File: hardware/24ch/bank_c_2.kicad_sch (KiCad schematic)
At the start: 45 parts, among them U301 AD7124-8BCPZ, U302 ADT7310TRZ, U303 ADT7310TRZ

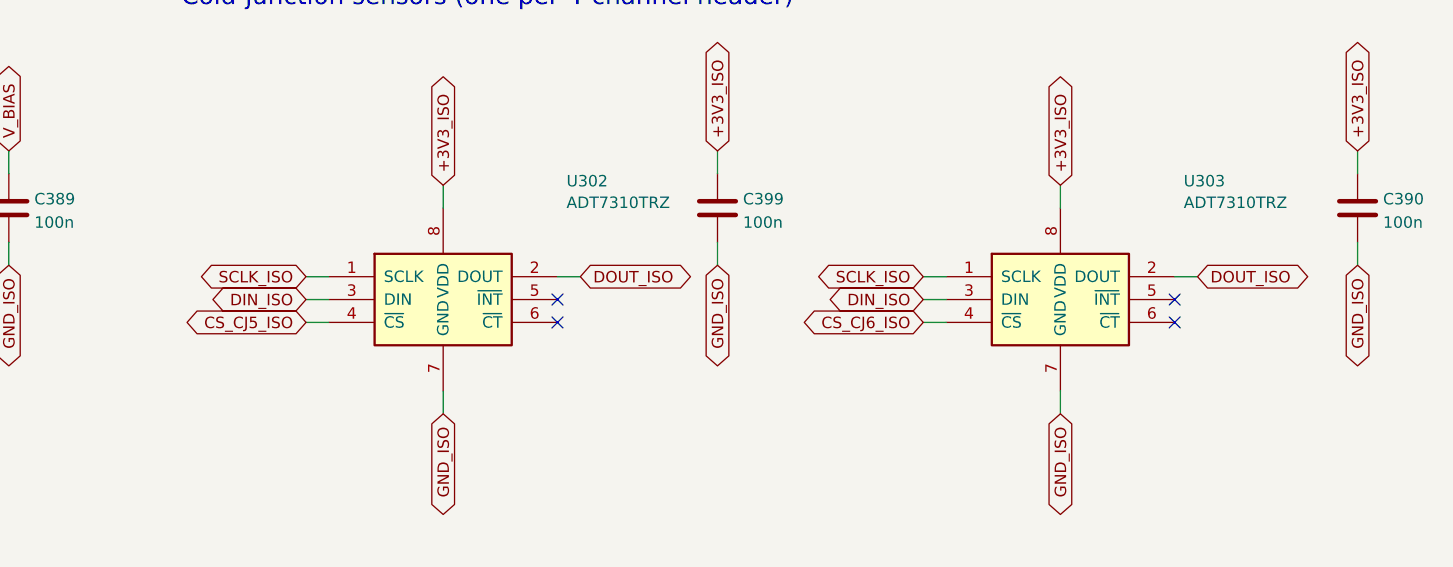
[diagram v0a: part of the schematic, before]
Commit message: 24ch cheaper-parts variant (0036): TMP126, CA-IS3761HW, RS-485 DNP, drop-in swaps
- CJ sensors ADT7310 x6 -> TMP126DCKR (C5219998); R443 22k DIN_ISO-DOUT_ISO for the
  3-wire SIO, R415 removed, ALERT grounded. Sensors moved <= 8 mm to clear spots beside
  their 100 nF (no closer spot to the terminals without touching TC traces, 0035 D2).
- ISO7761 -> CA-IS3761HW (same pinout, 5F/1R, default high); BOCHEN 3296W trimmer;
  SAMWHA 22u 1210.
- RS-485 block DNP: footprints kept; fab.py drops DNP parts from BOM/CPL and writes
  DNP.txt; cost.py skips them. External window watchdog tried and removed (owner).
- gen/delta.py: carry a schematic change onto the routed board (replace/add/remove,
  re-net, DNP, OLD>NEW@DEG reuse); it never deletes another net's track under a pad.
- Board: incremental edits only; analog nets (TC*, V_BIAS, VREF, REF*) identical to
  the pre-0036 board. Gates: ERC 0/0 (471 symbols); fab.py DRC/unconnected/parity
  0/0/0; pincaps 0 over. Parts ~$105 -> ~$72/board (CALCULATIONS 8.1, by hand).
- Docs: decision 0036, CALCULATIONS 8, ISSUES (I-109, I-114, I-119, I-104, I-094,
  new I-123 stock), STATE, 24ch README, superseded.txt.

Co-Authored-By: Claude Opus 5.5 <noreply@anthropic.com>
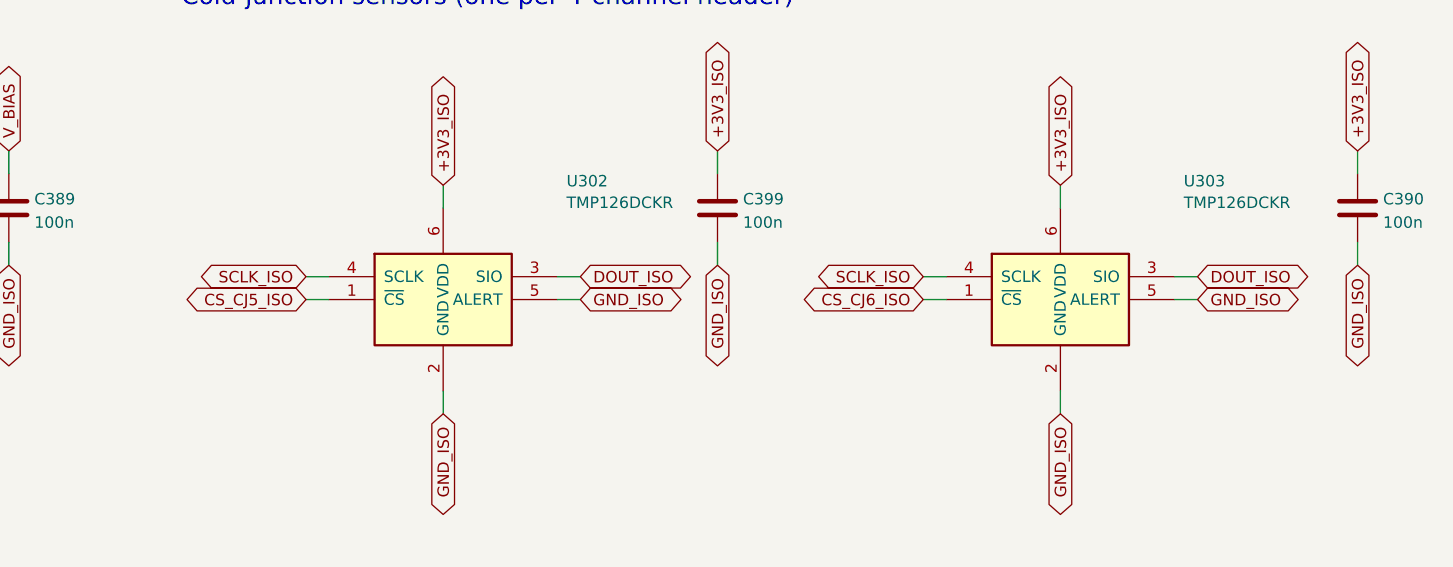
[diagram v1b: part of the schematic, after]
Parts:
- U302, U303: value ADT7310TRZ -> TMP126DCKR; footprint Package_SO:SOIC-8_3.9x4.9mm_P1.27mm -> Package_TO_SOT_SMD:SOT-363_SC-70-6; symbol thermo24:ADT7310 -> thermo24:TMP126; LCSC C578060 -> C5219998; MPN ADT7310TRZ-REEL7 -> TMP126DCKR; Manufacturer ADI -> TI
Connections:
- net +3V3_ISO: now also U302.6 (VDD), U303.6 (VDD); no longer U302.8 (VDD), U303.8 (VDD)
- net CS_CJ5_ISO: now also U302.1 (~{CS}); no longer U302.4 (~{CS})
- net CS_CJ6_ISO: now also U303.1 (~{CS}); no longer U303.4 (~{CS})
- net DIN_ISO: no longer U302.3 (DIN), U303.3 (DIN)
- net DOUT_ISO: now also U302.3 (SIO), U303.3 (SIO); no longer U302.2 (DOUT), U303.2 (DOUT)
- net GND_ISO: now also U302.2 (GND), U302.5 (ALERT), U303.2 (GND), U303.5 (ALERT); no longer U302.7 (GND), U303.7 (GND)
- net SCLK_ISO: now also U302.4 (SCLK), U303.4 (SCLK); no longer U302.1 (SCLK), U303.1 (SCLK)
- no-connect marks 6 -> 2
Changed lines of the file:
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@@
 	)
 	(symbol
-		(lib_id "thermo24:ADT7310")
+		(lib_id "thermo24:TMP126")
 		(at 254 185.42 0)
 		(unit 1)
@@
 			)
 		)
-		(property "Value" "ADT7310TRZ"
+		(property "Value" "TMP126DCKR"
 			(at 267.7 174.66 0)
 			(effects
@@
 			)
 		)
-		(property "Footprint" "Package_SO:SOIC-8_3.9x4.9mm_P1.27mm"
+		(property "Footprint" "Package_TO_SOT_SMD:SOT-363_SC-70-6"
 			(at 254 185.42 0)
 			(effects
@@
 			)
 		)
-		(property "Description" "cold junction at the seam of header J301"
+		(property "Description" "cold junction at header J301; SIO on DOUT, written through R443; ALERT unused, grounded (datasheet allows) (0036)"
 			(at 254 185.42 0)
 			(effects
@@
 			)
 		)
-		(property "MPN" "ADT7310TRZ-REEL7"
+		(property "MPN" "TMP126DCKR"
 			(at 254 185.42 0)
 			(effects
@@
 			)
 		)
-		(property "Manufacturer" "ADI"
+		(property "Manufacturer" "TI"
 			(at 254 185.42 0)
 			(effects
@@
 			)
 		)
-		(property "LCSC" "C578060"
+		(property "LCSC" "C5219998"
 			(at 254 185.42 0)
 			(effects
@@
 			)
 		)
+		(pin "4"
+		)
 		(pin "1"
 		)
 		(pin "3"
 		)
-		(pin "4"
+		(pin "5"
+		)
+		(pin "6"
 		)
 		(pin "2"
-		)
-		(pin "5"
-		)
-		(pin "6"
-		)
-		(pin "8"
-		)
-		(pin "7"
 		)
 		(instances
@@
 		)
 	)
-	(global_label "DIN_ISO"
+	(global_label "CS_CJ5_ISO"
 		(shape bidirectional)
 		(at 238.76 185.42 180)
@@
 		(property "Intersheetrefs" "${INTERSHEET_REFS}"
 			(at 238.76 185.42 0)
-			(effects
-				(font
-					(size 1.27 1.27)
-				)
-				(hide yes)
-			)
-		)
-	)
-	(wire
-		(pts
-			(xy 241.3 187.96)
-			(xy 238.76 187.96)
-		)
-		(stroke
-			(width 0)
-			(type default)
-		)
-	)
-	(global_label "CS_CJ5_ISO"
-		(shape bidirectional)
-		(at 238.76 187.96 180)
-		(fields_autoplaced yes)
-		(effects
-			(font
-				(size 1.27 1.27)
-			)
-			(justify right)
-		)
-		(property "Intersheetrefs" "${INTERSHEET_REFS}"
-			(at 238.76 187.96 0)
 			(effects
 				(font
@@
 		)
 	)
-	(no_connect
-		(at 266.7 185.42)
-	)
-	(no_connect
-		(at 266.7 187.96)
+	(wire
+		(pts
+			(xy 266.7 185.42)
+			(xy 269.24 185.42)
+		)
+		(stroke
+			(width 0)
+			(type default)
+		)
+	)
+	(global_label "GND_ISO"
+		(shape bidirectional)
+		(at 269.24 185.42 0)
+		(fields_autoplaced yes)
+		(effects
+			(font
+				(size 1.27 1.27)
+			)
+			(justify left)
+		)
+		(property "Intersheetrefs" "${INTERSHEET_REFS}"
+			(at 269.24 185.42 0)
+			(effects
+				(font
+					(size 1.27 1.27)
+				)
+				(hide yes)
+			)
+		)
 	)
 	(wire
@@
 	)
 	(symbol
-		(lib_id "thermo24:ADT7310")
+		(lib_id "thermo24:TMP126")
 		(at 322.58 185.42 0)
 		(unit 1)
@@
 			)
 		)
-		(property "Value" "ADT7310TRZ"
+		(property "Value" "TMP126DCKR"
 			(at 336.28 174.66 0)
 			(effects
@@
 			)
 		)
-		(property "Footprint" "Package_SO:SOIC-8_3.9x4.9mm_P1.27mm"
+		(property "Footprint" "Package_TO_SOT_SMD:SOT-363_SC-70-6"
 			(at 322.58 185.42 0)
 			(effects
@@
 			)
 		)
-		(property "Description" "cold junction at the seam of header J302"
+		(property "Description" "cold junction at header J302; SIO on DOUT, written through R443; ALERT unused, grounded (datasheet allows) (0036)"
 			(at 322.58 185.42 0)
 			(effects
@@
 			)
 		)
-		(property "MPN" "ADT7310TRZ-REEL7"
+		(property "MPN" "TMP126DCKR"
 			(at 322.58 185.42 0)
 			(effects
@@
 			)
 		)
-		(property "Manufacturer" "ADI"
+		(property "Manufacturer" "TI"
 			(at 322.58 185.42 0)
 			(effects
@@
 			)
 		)
-		(property "LCSC" "C578060"
+		(property "LCSC" "C5219998"
 			(at 322.58 185.42 0)
 			(effects
@@
 			)
 		)
+		(pin "4"
+		)
 		(pin "1"
 		)
 		(pin "3"
 		)
-		(pin "4"
+		(pin "5"
+		)
+		(pin "6"
 		)
 		(pin "2"
-		)
-		(pin "5"
-		)
-		(pin "6"
-		)
-		(pin "8"
-		)
-		(pin "7"
 		)
 		(instances
@@
 		)
 	)
-	(global_label "DIN_ISO"
+	(global_label "CS_CJ6_ISO"
 		(shape bidirectional)
 		(at 307.34 185.42 180)
@@
 		(property "Intersheetrefs" "${INTERSHEET_REFS}"
 			(at 307.34 185.42 0)
-			(effects
-				(font
-					(size 1.27 1.27)
-				)
-				(hide yes)
-			)
-		)
-	)
-	(wire
-		(pts
-			(xy 309.88 187.96)
-			(xy 307.34 187.96)
-		)
-		(stroke
-			(width 0)
-			(type default)
-		)
-	)
-	(global_label "CS_CJ6_ISO"
-		(shape bidirectional)
-		(at 307.34 187.96 180)
-		(fields_autoplaced yes)
-		(effects
-			(font
-				(size 1.27 1.27)
-			)
-			(justify right)
-		)
-		(property "Intersheetrefs" "${INTERSHEET_REFS}"
-			(at 307.34 187.96 0)
 			(effects
 				(font
@@
 		)
 	)
-	(no_connect
-		(at 335.28 185.42)
-	)
-	(no_connect
-		(at 335.28 187.96)
-	)
-	(wire
+	(wire
+		(pts
+			(xy 335.28 185.42)
+			(xy 337.82 185.42)
+		)
+		(stroke
+			(width 0)
+			(type default)
+		)
+	)
+	(global_label "GND_ISO"
+		(shape bidirectional)
+		(at 337.82 185.42 0)
+		(fields_autoplaced yes)
+		(effects
+			(font
+				(size 1.27 1.27)
+			)
+			(justify left)
+		)
+		(property "Intersheetrefs" "${INTERSHEET_REFS}"
+			(at 337.82 185.42 0)
+			(effects
+				(font
+					(size 1.27 1.27)
+				)
+				(hide yes)
+			)
+		)
+	)
+	(wire
